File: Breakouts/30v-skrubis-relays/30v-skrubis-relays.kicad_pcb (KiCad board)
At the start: 2 copper layers, 40 x 11 mm, 13 parts, among them J1 Conn_01x03, J2 Conn_01x01, J4 Conn_01x01, J5 Conn_01x02, K1 G5Q-1A, Q1 Q_PNP_BEC, U1 PC817

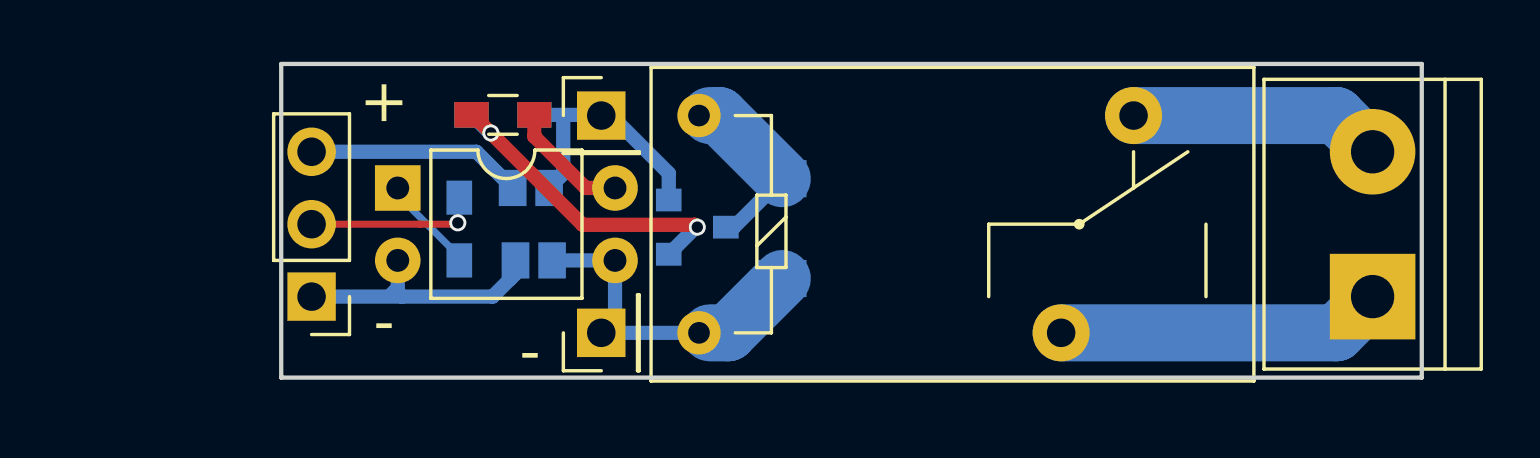
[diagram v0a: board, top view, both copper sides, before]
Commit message: Changing the 48V relay breakout board so that all the SMD components are mounted on the bottom side => easier to assemble
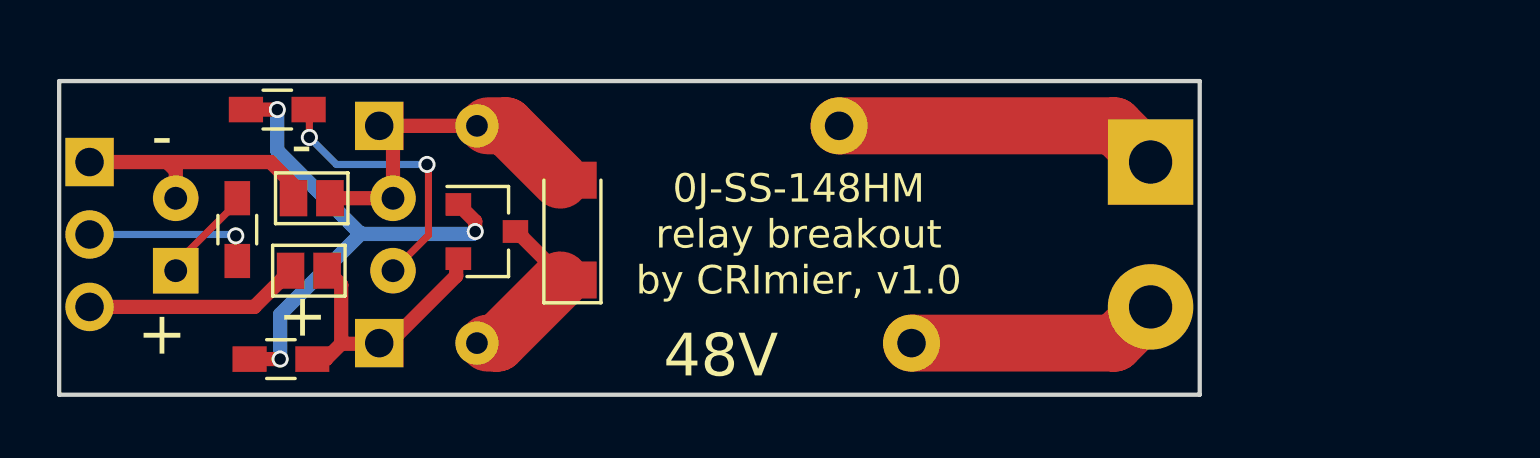
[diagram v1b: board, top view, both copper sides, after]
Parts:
- D1, JP1, JP2, Q1: moved to F.Cu
- J1, J2, J4, J5, K1, U1: moved to B.Cu
- R1: value 1k -> 1K; moved to F.Cu
- R2: value 1k -> 50K; moved to F.Cu
- R3: value 1k -> 10K
- moved R2 11.6 mm to (132.3, 114.0)
- moved J4 11.2 mm to (135.7, 113.4)
- moved K1 10.6 mm to (139.2, 105.8)
- moved J2 10.6 mm to (135.7, 105.8), turned to 270 degrees
- moved J1 9.11 mm to (125.6, 107.0)
- moved J5 9.11 mm to (162.8, 107.0), turned to 270 degrees
- moved JP1 8.31 mm to (133.3, 110.9), turned to 90 degrees
- moved U1 8.31 mm to (128.6, 110.9)
- moved JP2 8.09 mm to (133.4, 108.3), turned to 90 degrees
- moved R3 7.92 mm to (132.1, 105.2)
- moved R1 7.79 mm to (130.7, 109.4), turned to 270 degrees
- moved Q1 7.38 mm to (139.5, 109.5)
- moved D1 7.36 mm to (142.5, 109.4), turned to 90 degrees
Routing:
- net Net-(Q1-Pad1): track 12.0 -> 18.6 mm, vias 2 -> 3
- net Net-(R3-Pad2): track 4.34 -> 9.76 mm, vias 0 -> 2
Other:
- board text added: "48V"
